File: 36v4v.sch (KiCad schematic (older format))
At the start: 34 parts, among them J1 Conn_01x03, J2 Conn_01x02, J3 Conn_01x02, U1 INN3162C-H1XX

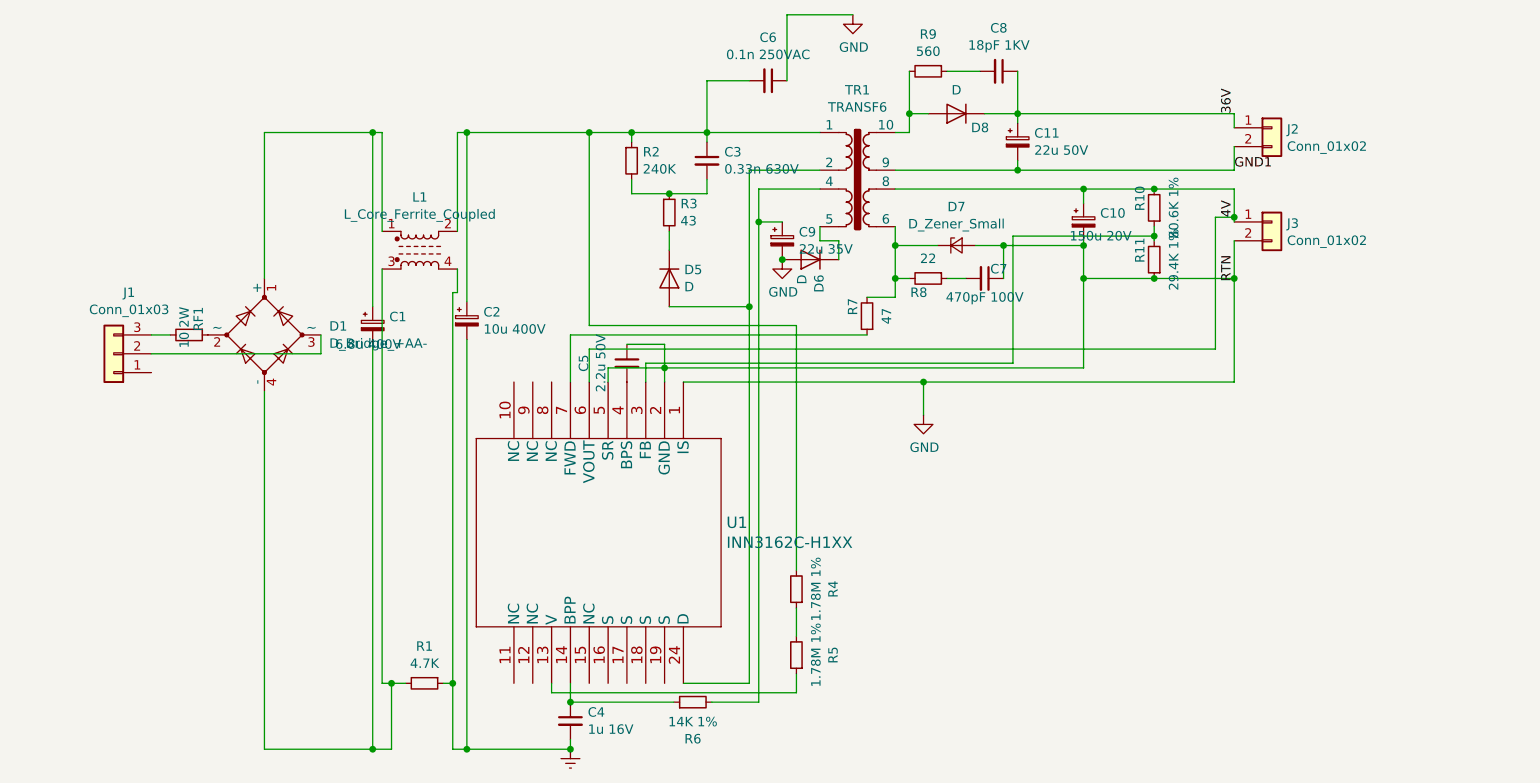
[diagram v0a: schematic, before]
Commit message: Incorporated Anil's feedback, BOM
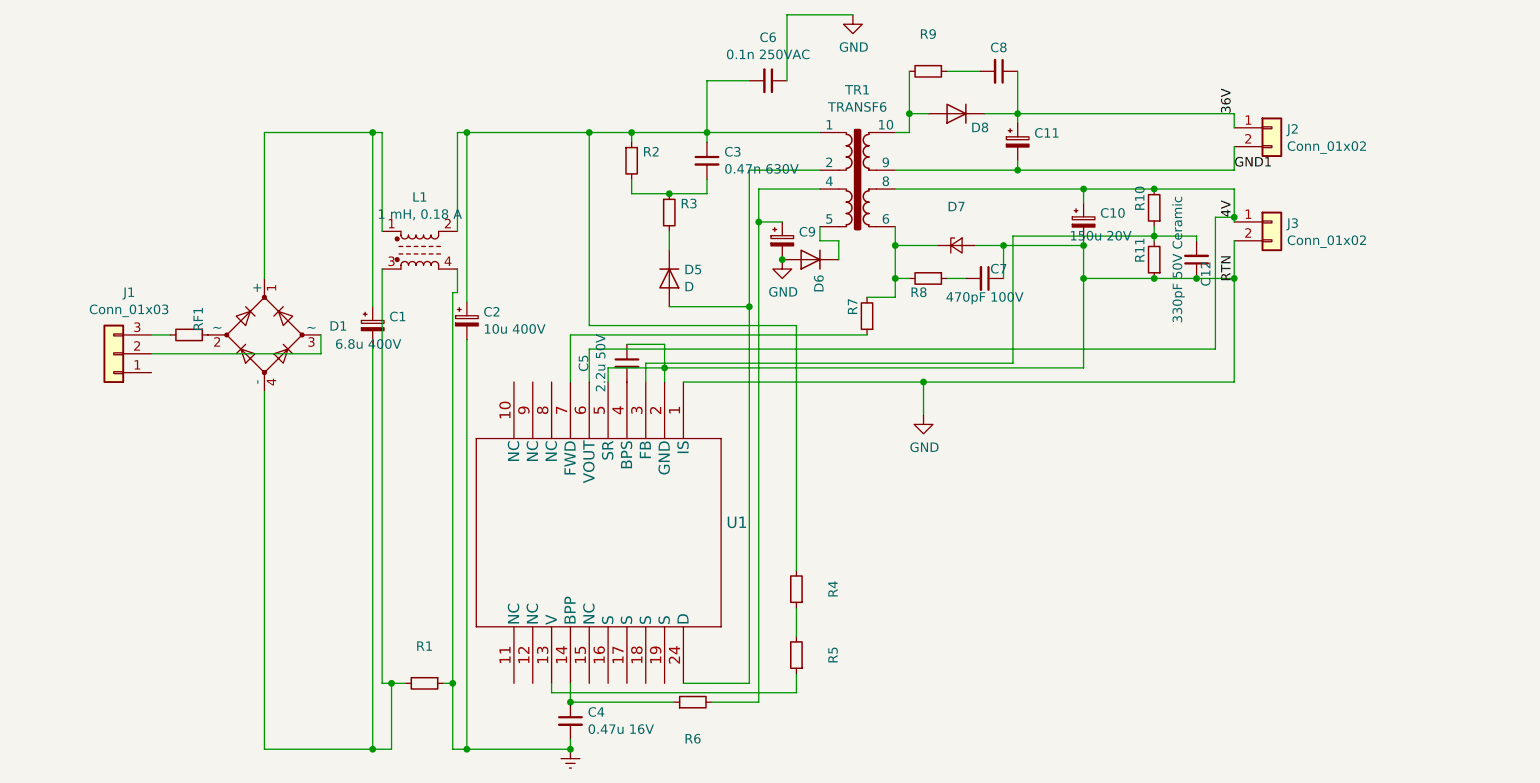
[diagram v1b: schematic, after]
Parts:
- added C12: 330pF 50V Ceramic, Capacitor_THT:CP_Radial_D10.0mm_P5.00mm, symbol Device:C_Small
- C1, C2: MFG Name (none) -> Panasonic; MFG Part Num (none) -> EEV-EB2G100SM
- C10: MFG Name (none) -> Nichikon; MFG Part Num (none) -> PLF1D151MDO2TD
- C11: value 22u 50V -> 22u 50V Electrolytic; MFG Name (none) -> United Chemi-Con; MFG Part Num (none) -> EKZE500ELL220ME11D
- C3: value 0.33n 630V -> 0.47n 630V; MFG Name (none) -> Murata; MFG Part Num (none) -> RCE7U2J471J2M1H03A
- C4: value 1u 16V -> 0.47u 16V; MFG Name (none) -> TDK; MFG Part Num (none) -> FK18X7R1C474K
- C5: MFG Name (none) -> Kemet; MFG Part Num (none) -> C340C225K5R5TA
- C6: MFG Name (none) -> Vishay Cera-Mite; MFG Part Num (none) -> 440LT10-R
- C7: MFG Name (none) -> Vishay; MFG Part Num (none) -> K471J15C0GH5TH5
- C8: value 18pF 1KV -> 18pF 1KV Ceramic; MFG Name (none) -> Panasonic; MFG Part Num (none) -> ECC-D3A180JGE
- C9: value 22u 35V -> 22u 35V Electrolytic; MFG Name (none) -> Panasonic; MFG Part Num (none) -> EEU-FC1V220H
- D1: value D_Bridge_+AA- -> D_Bridge_+AA- / 800 V, 1 A, Standard Recovery, DO-41; MFG Name (none) -> Vishay; MFG Part Num (none) -> 1N4006-E3/54
- D6: value D -> 150 V, 0.2 A, Standard Recovery, DO-35; MFG Name (none) -> ON Semi; MFG Part Num (none) -> 1N3595TR
- D7: value D_Zener_Small -> 40 V, 2 A, Schottky, DO-15; MFG Name (none) -> Vishay; MFG Part Num (none) -> SB240-E3/54
- D8: value D -> 400 V, 1 A, Ultrafast Recovery, 30 ns, SOD57; MFG Name (none) -> Phillips; MFG Part Num (none) -> BYV26B-TR
- L1: value L_Core_Ferrite_Coupled -> 1 mH, 0.18 A; MFG Name (none) -> Kemet; MFG Part Num (none) -> SBC2-102-181
- R1: value 4.7K -> 4.7 kΩ, 5 %, 0.25 W, Carbon Film
- R10: value 80.6K 1% -> 80.6 kΩ, 1 %, 0.125 W, Metal Film
- R11: value 29.4K 1% -> 29.4 kΩ, 1 %, 0.125 W, Metal Film
- R2: value 240K -> 240 kΩ, 5 %, 0.25 W, Carbon Film
- R3: value 43 -> 43 Ω, 5 %, 0.125 W, Carbon Film
- R4, R5: value 1.78M 1% -> 1.78 MΩ, 1 %, 0.25 W, Metal Film
- R6: value 14K 1% -> 14 kΩ, 1 %, 0.125 W, Metal Film
- R7: value 47 -> 47 Ω, 5 %, 0.125 W, Carbon Film
- R8: value 22 -> 22 Ω, 5 %, 0.25 W, Carbon Film
- R9: value 560 -> 560 Ω, 5 %, 0.25 W, Carbon Film
- RF1: value 10 2W -> 10 Ω, 2 W, Flameproof Wire-Wound Resistor
- U1: value INN3162C-H1XX -> InnoSwitch3-CE, INN3162C, inSOP-24D; MFG Name (none) -> Power Integrations; MFG Part Num (none) -> INN3162C-H101
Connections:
- net GND: now also C12.1
- net at R10.1, R11.2, U1.3 (FB): now also C12.2

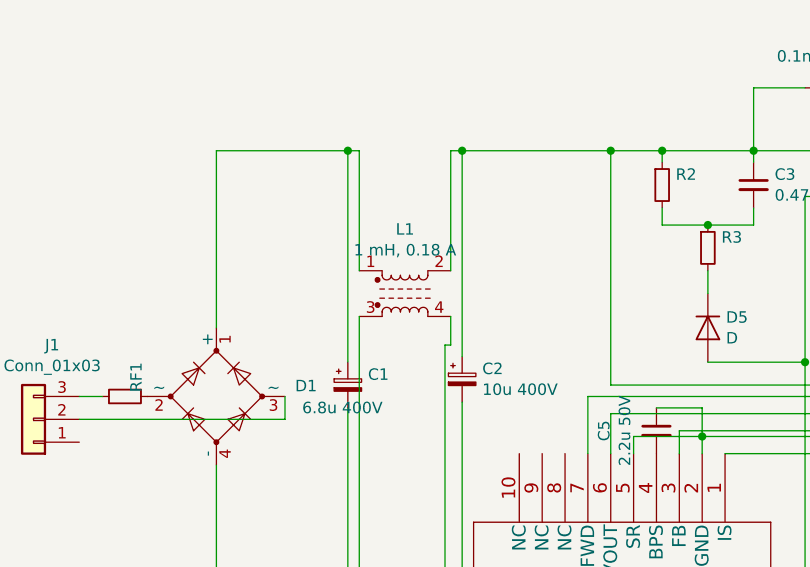
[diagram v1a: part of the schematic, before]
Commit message: Changed cap footprints, layout. Added datasheets
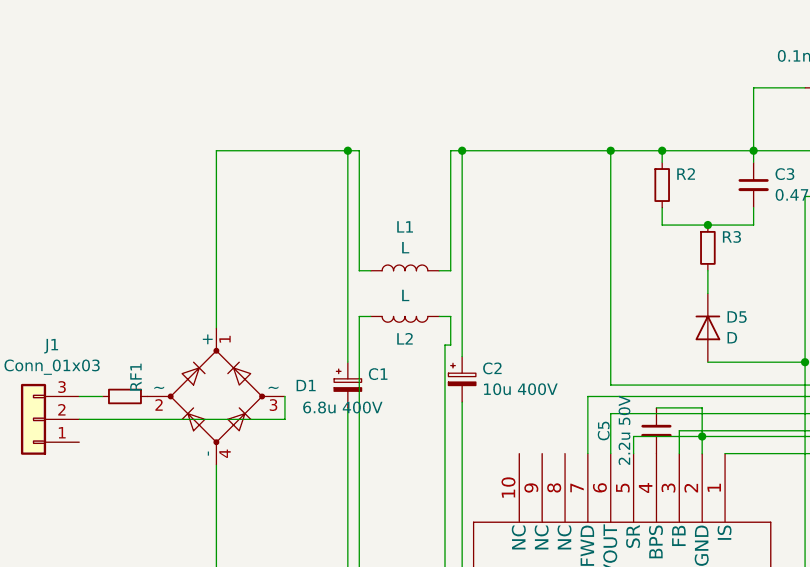
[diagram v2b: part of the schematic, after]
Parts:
- removed L1: 1 mH, 0.18 A, Inductor_THT:Choke_Schaffner_RN202-04-8.8x18.2mm, symbol Device:L_Core_Ferrite_Coupled
- added L1, L2: L, Inductor_THT:L_Radial_D6.0mm_P4.00mm, symbol Device:L
- C1: footprint Capacitor_THT:CP_Radial_D8.0mm_P5.00mm -> pwrcon:CP_Elec_EEV_16x17.5
- C12: footprint Capacitor_THT:CP_Radial_D10.0mm_P5.00mm -> Capacitor_THT:CP_Radial_D8.0mm_P5.00mm
- C2: footprint Capacitor_THT:CP_Radial_D14.0mm_P7.50mm -> pwrcon:CP_Elec_EEV_16x17.5
- C3: footprint Capacitor_SMD:C_0603_1608Metric_Pad1.05x0.95mm_HandSolder -> Capacitor_THT:CP_Radial_Tantal_D5.5mm_P5.00mm
- D1: footprint Diode_SMD:Diode_Bridge_Bourns_CD-DF4xxS -> Diode_THT:Diode_Bridge_Vishay_GBL; MFG Part Num 1N4006-E3/54 -> GBL06-E3/45GI-ND OR 1N4006-E3/54
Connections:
- net Earth: now also L2.1
- net at C1.1, D1.1 (+): now also L1.1
- net at C1.2, D1.4 (-), R1.2: now also L2.2
- net at C2.1, C3.1, C6.2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: now also L1.2
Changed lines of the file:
@@
 F 0 "C1" H 3488 2521 50  0000 L CNN
 F 1 "6.8u 400V" H 3200 2375 50  0000 L CNN
-F 2 "Capacitor_THT:CP_Radial_D8.0mm_P5.00mm" H 3400 2475 50  0001 C CNN
+F 2 "pwrcon:CP_Elec_EEV_16x17.5" H 3400 2475 50  0001 C CNN
 F 3 "~" H 3400 2475 50  0001 C CNN
 F 4 "Panasonic" H 3400 2475 50  0001 C CNN "MFG Name"
@@
 F 0 "C2" H 3988 2496 50  0000 L CNN
 F 1 "10u 400V" H 3988 2405 50  0000 L CNN
-F 2 "Capacitor_THT:CP_Radial_D14.0mm_P7.50mm" H 3900 2450 50  0001 C CNN
+F 2 "pwrcon:CP_Elec_EEV_16x17.5" H 3900 2450 50  0001 C CNN
 F 3 "~" H 3900 2450 50  0001 C CNN
 F 4 "Panasonic" H 3900 2450 50  0001 C CNN "MFG Name"
@@
 F 0 "C3" H 5267 1646 50  0000 L CNN
 F 1 "0.47n 630V" H 5267 1555 50  0000 L CNN
-F 2 "Capacitor_SMD:C_0603_1608Metric_Pad1.05x0.95mm_HandSolder" H 5175 1600 50  0001 C CNN
+F 2 "Capacitor_THT:CP_Radial_Tantal_D5.5mm_P5.00mm" H 5175 1600 50  0001 C CNN
 F 3 "~" H 5175 1600 50  0001 C CNN
 F 4 "Murata" H 5175 1600 50  0001 C CNN "MFG Name"
@@
 Connection ~ 6325 2775
 Connection ~ 7975 2225
-$Comp
-L Device:L_Core_Ferrite_Coupled L1
-U 1 1 5E76A187
-P 3650 2075
-F 0 "L1" H 3650 2356 50  0000 C CNN
-F 1 "1 mH, 0.18 A" H 3650 2265 50  0000 C CNN
-F 2 "Inductor_THT:Choke_Schaffner_RN202-04-8.8x18.2mm" H 3650 2075 50  0001 C CNN
-F 3 "~" H 3650 2075 50  0001 C CNN
-F 4 "Kemet" H 3650 2075 50  0001 C CNN "MFG Name"
-F 5 "SBC2-102-181" H 3650 2075 50  0001 C CNN "MFG Part Num"
-	1    3650 2075
-	1    0    0    -1
-$EndComp
 Wire Wire Line
 	3450 1975 3450 1450
@@
 F 0 "D1" V 2871 2181 50  0000 R CNN
 F 1 "D_Bridge_+AA- / 800 V, 1 A, Standard Recovery, DO-41 " V 2780 2181 50  0001 R CNN
-F 2 "Diode_SMD:Diode_Bridge_Bourns_CD-DF4xxS" H 2825 2525 50  0001 C CNN
+F 2 "Diode_THT:Diode_Bridge_Vishay_GBL" H 2825 2525 50  0001 C CNN
 F 3 "~" H 2825 2525 50  0001 C CNN
 F 4 "Vishay" H 2825 2525 50  0001 C CNN "MFG Name"
-F 5 "1N4006-E3/54" H 2825 2525 50  0001 C CNN "MFG Part Num"
+F 5 "GBL06-E3/45GI-ND OR 1N4006-E3/54" H 2825 2525 50  0001 C CNN "MFG Part Num"
 	1    2825 2525
 	0    -1   -1   0
@@
 F 0 "C12" V 7725 2200 50  0000 C CNN
 F 1 "330pF 50V Ceramic" V 7875 2125 50  0000 C CNN
-F 2 "Capacitor_THT:CP_Radial_D10.0mm_P5.00mm" H 7775 2125 50  0001 C CNN
+F 2 "Capacitor_THT:CP_Radial_D8.0mm_P5.00mm" H 7775 2125 50  0001 C CNN
 F 3 "~" H 7775 2125 50  0001 C CNN
 F 4 "Vishay" H 7775 2125 50  0001 C CNN "MFG Name"
@@
 Wire Wire Line
 	7775 2000 7775 2025
+$Comp
+L Device:L L1
+U 1 1 5E810FBB
+P 3650 1975
+F 0 "L1" V 3840 1975 50  0000 C CNN
+F 1 "L" V 3749 1975 50  0000 C CNN
+F 2 "Inductor_THT:L_Radial_D6.0mm_P4.00mm" H 3650 1975 50  0001 C CNN
+F 3 "~" H 3650 1975 50  0001 C CNN
+F 4 "Kemet" H 3650 1975 50  0001 C CNN "MFG Name"
+F 5 "SBC2-102-181" H 3650 1975 50  0001 C CNN "MFG Part Num"
+	1    3650 1975
+	0    -1   -1   0
+$EndComp
+$Comp
+L Device:L L2
+U 1 1 5E811748
+P 3650 2175
+F 0 "L2" V 3750 2175 50  0000 C CNN
+F 1 "L" V 3560 2175 50  0000 C CNN
+F 2 "Inductor_THT:L_Radial_D6.0mm_P4.00mm" H 3650 2175 50  0001 C CNN
+F 3 "~" H 3650 2175 50  0001 C CNN
+F 4 "Kemet" H 3650 2175 50  0001 C CNN "MFG Name"
+F 5 "SBC2-102-181" H 3650 2175 50  0001 C CNN "MFG Part Num"
+	1    3650 2175
+	0    1    1    0
+$EndComp
+Wire Wire Line
+	3450 1975 3500 1975
+Wire Wire Line
+	3800 1975 3850 1975
+Wire Wire Line
+	3450 2175 3500 2175
+Wire Wire Line
+	3800 2175 3850 2175
 $EndSCHEMATC

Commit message: Changed pcz size, modified footprints
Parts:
- added J4, J5: Conn_01x02, Connector_Wire:SolderWirePad_1x02_P5.08mm_Drill1.5mm, symbol Connector_Generic:Conn_01x02
- C11: footprint Capacitor_THT:CP_Radial_D10.0mm_P5.00mm -> Capacitor_THT:CP_Radial_D5.0mm_P2.00mm
- J1: footprint Connector_PinHeader_2.54mm:PinHeader_1x03_P2.54mm_Vertical -> Connector_Phoenix_MC_HighVoltage:PhoenixContact_MCV_1,5_3-G-5.08_1x03_P5.08mm_Vertical
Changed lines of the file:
@@
 F 0 "C11" H 6913 1546 50  0000 L CNN
 F 1 "22u 50V Electrolytic" H 6913 1455 50  0001 L CNN
-F 2 "Capacitor_THT:CP_Radial_D10.0mm_P5.00mm" H 6825 1500 50  0001 C CNN
+F 2 "Capacitor_THT:CP_Radial_D5.0mm_P2.00mm" H 6825 1500 50  0001 C CNN
 F 3 "~" H 6825 1500 50  0001 C CNN
 F 4 "United Chemi-Con" H 6825 1500 50  0001 C CNN "MFG Name"
@@
 F 0 "J1" H 1943 2300 50  0000 C CNN
 F 1 "Conn_01x03" H 1943 2391 50  0000 C CNN
-F 2 "Connector_PinHeader_2.54mm:PinHeader_1x03_P2.54mm_Vertical" H 2025 2625 50  0001 C CNN
+F 2 "Connector_Phoenix_MC_HighVoltage:PhoenixContact_MCV_1,5_3-G-5.08_1x03_P5.08mm_Vertical" H 2025 2625 50  0001 C CNN
 F 3 "~" H 2025 2625 50  0001 C CNN
 	1    2025 2625
@@
 Wire Wire Line
 	3800 2175 3850 2175
+$Comp
+L Connector_Generic:Conn_01x02 J4
+U 1 1 5E906E27
+P 8250 2725
+F 0 "J4" H 8330 2717 50  0000 L CNN
+F 1 "Conn_01x02" H 8330 2626 50  0000 L CNN
+F 2 "Connector_Wire:SolderWirePad_1x02_P5.08mm_Drill1.5mm" H 8250 2725 50  0001 C CNN
+F 3 "~" H 8250 2725 50  0001 C CNN
+	1    8250 2725
+	1    0    0    -1
+$EndComp
+$Comp
+L Connector_Generic:Conn_01x02 J5
+U 1 1 5E909967
+P 8250 2375
+F 0 "J5" H 8330 2367 50  0000 L CNN
+F 1 "Conn_01x02" H 8330 2276 50  0000 L CNN
+F 2 "Connector_Wire:SolderWirePad_1x02_P5.08mm_Drill1.5mm" H 8250 2375 50  0001 C CNN
+F 3 "~" H 8250 2375 50  0001 C CNN
+	1    8250 2375
+	1    0    0    -1
+$EndComp
 $EndSCHEMATC
